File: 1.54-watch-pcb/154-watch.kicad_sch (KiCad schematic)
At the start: 64 parts, among them J1 AFC24-S24FIC-00, J2 Conn_01x06_Female, J3 USB_C_Programming, J4 Jack-DC, J5 Conn_01x02_Male, Q1 Si1308, Q2 BC817, Q3 BC817, Q4 Si2301CDS, SW1 RESET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

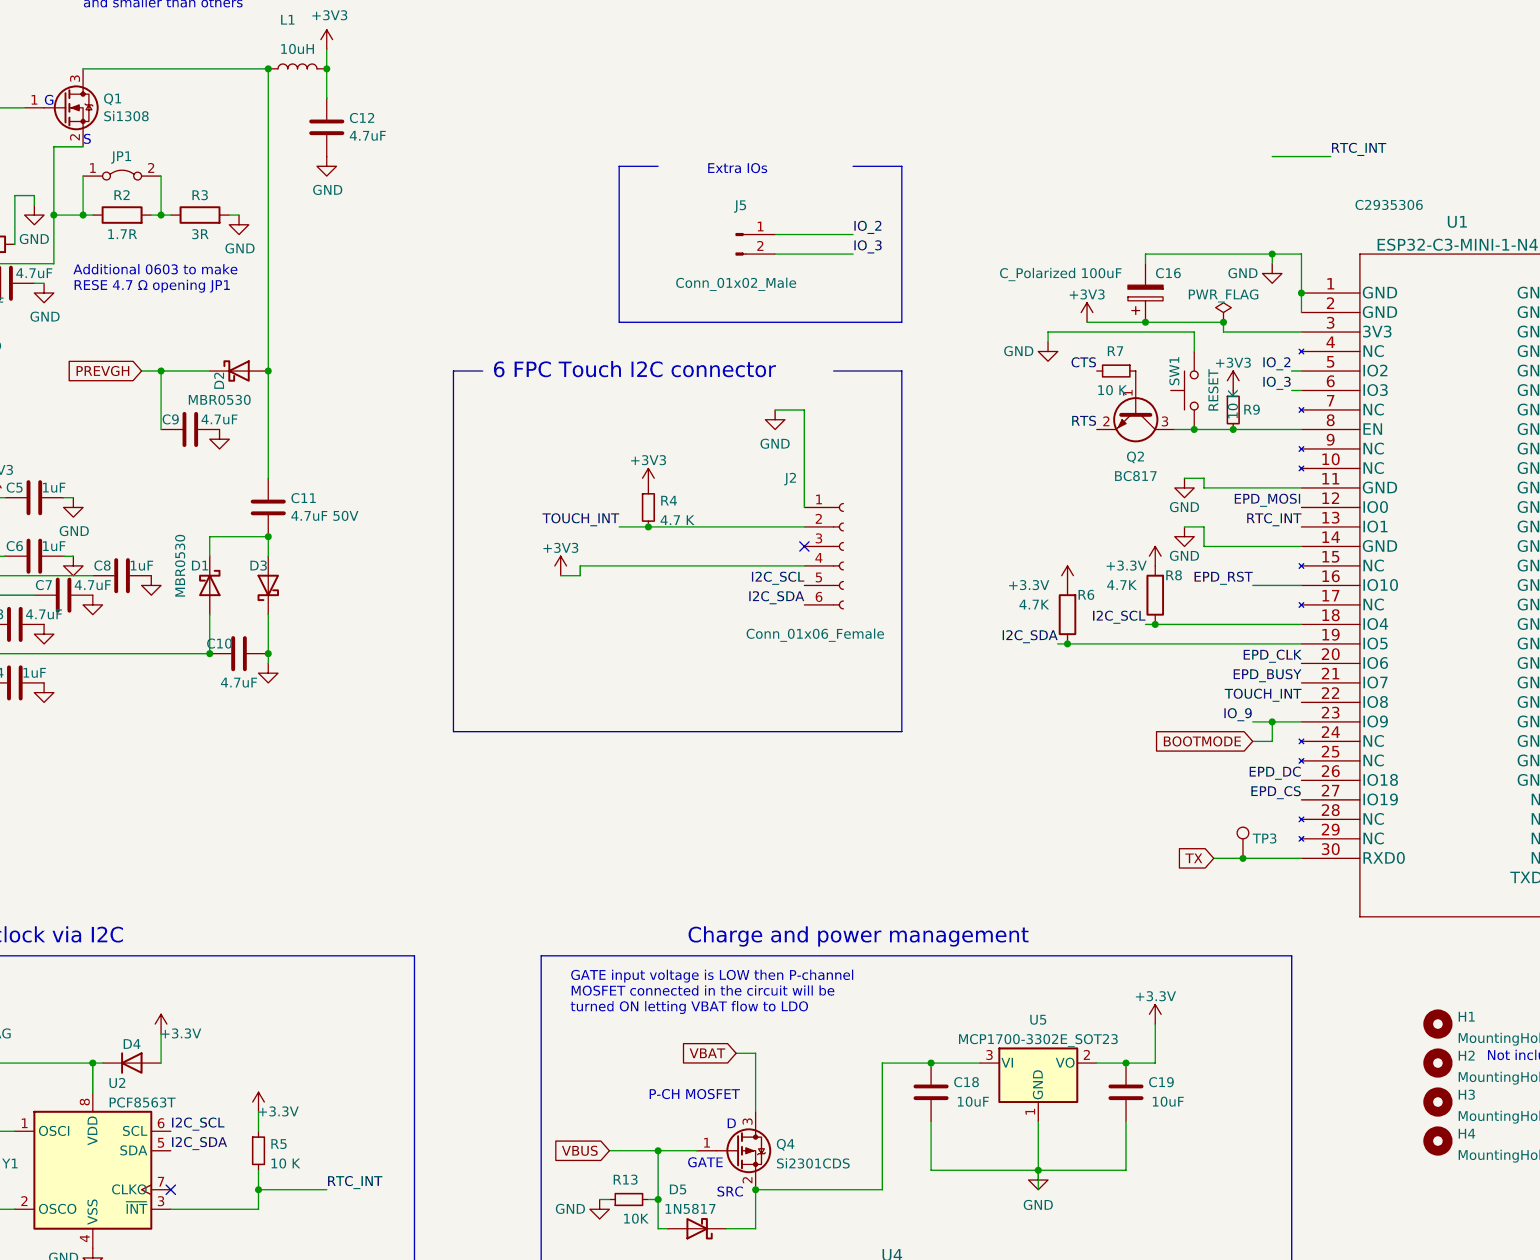
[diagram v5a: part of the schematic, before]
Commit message: First draft of LCD controller, non DRC val #10
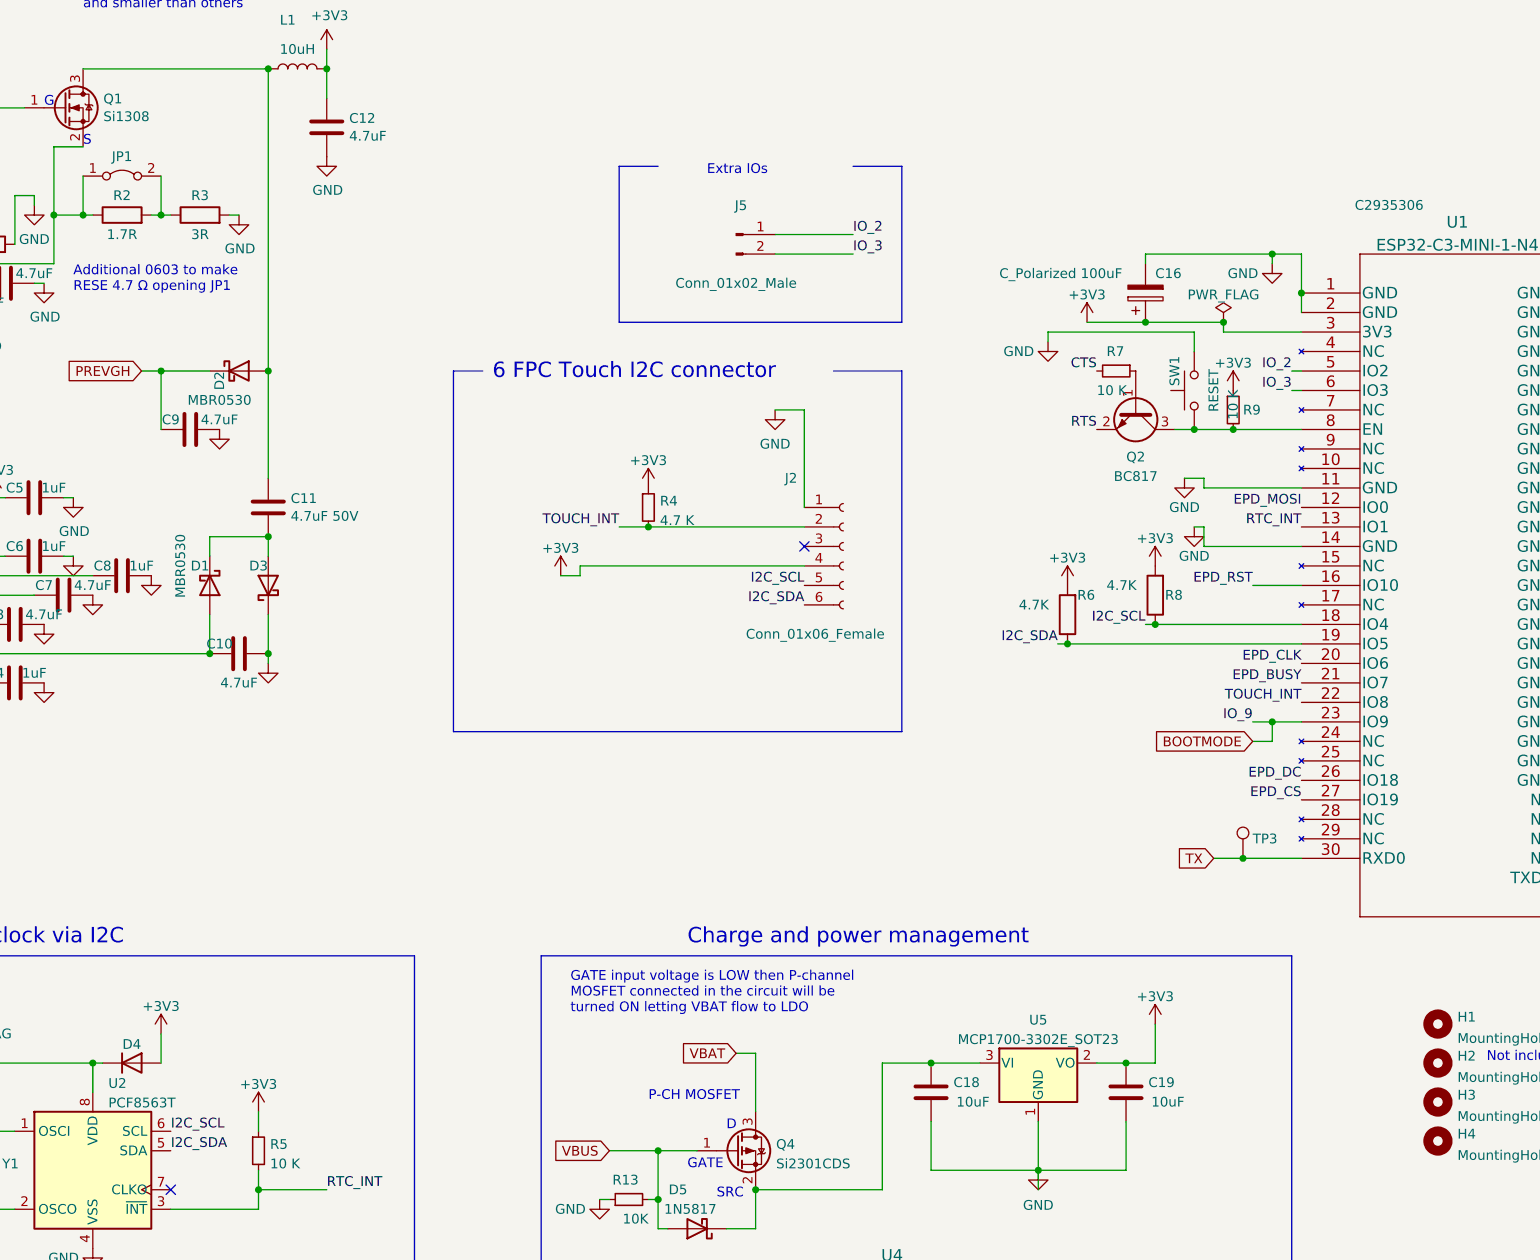
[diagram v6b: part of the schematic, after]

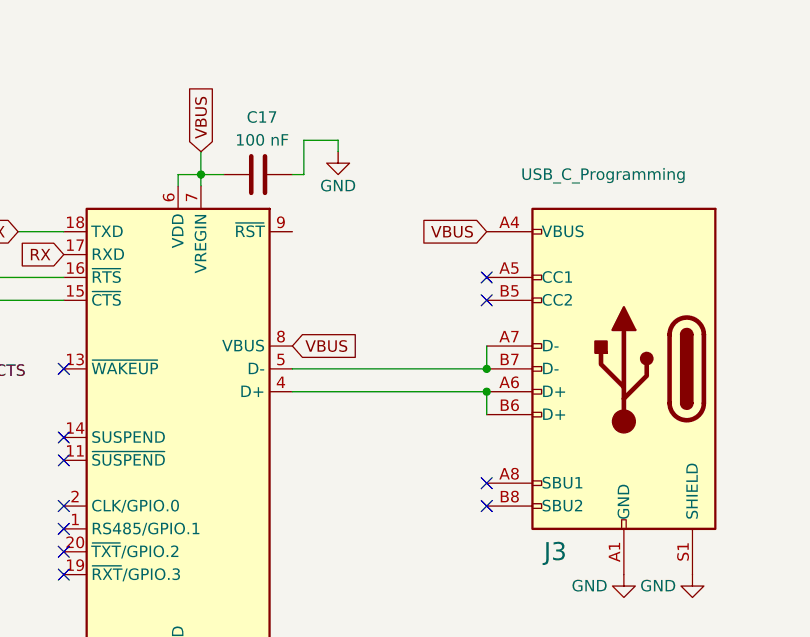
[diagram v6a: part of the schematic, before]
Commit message: Sharp LCD prod. 1.0 and update to failed watch
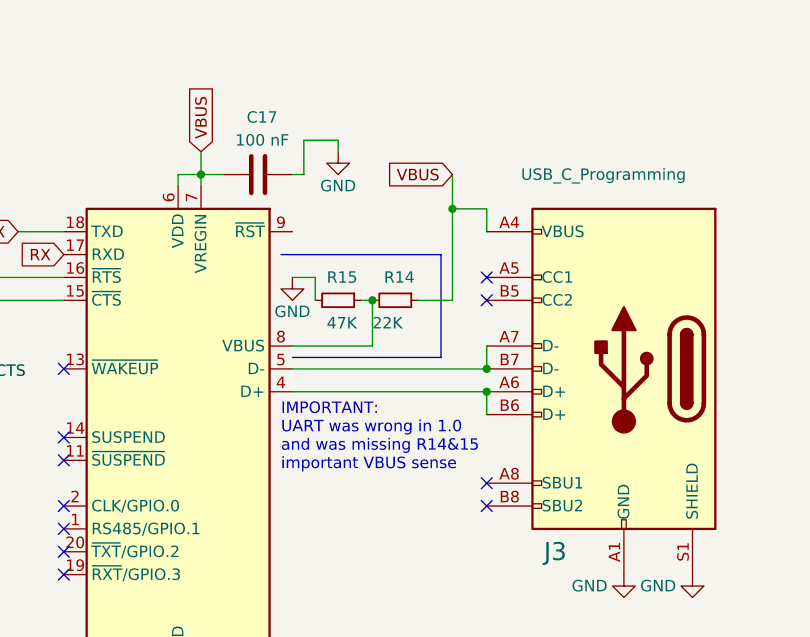
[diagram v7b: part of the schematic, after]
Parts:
- added R14: 22K, Resistor_SMD:R_0603_1608Metric, symbol Device:R_Small
- added R15: 47K, Resistor_SMD:R_0603_1608Metric, symbol Device:R_Small
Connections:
- net GND: now also R15.2
- net VBUS: now also R14.1; no longer U3.8 (VBUS)
- new net: R14.2, R15.1, U3.8 (VBUS)
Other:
- note added: "IMPORTANT: UART was wrong in 1.0 and was missing R14&15 important VBUS sense"
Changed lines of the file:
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@@
   (junction (at 281.94 92.71) (diameter 0) (color 0 0 0 0)
   )
+  (junction (at 372.11 62.23) (diameter 0) (color 0 0 0 0)
+  )
   (junction (at 281.94 123.19) (diameter 0) (color 0 0 0 0)
   )
@@
   (junction (at 281.94 69.85) (diameter 0) (color 0 0 0 0)
   )
+  (junction (at 363.22 72.39) (diameter 0) (color 0 0 0 0)
+  )
   (junction (at 281.94 67.31) (diameter 0) (color 0 0 0 0)
   )
@@
     (stroke (width 0) (type default))
   )
+  (wire (pts (xy 363.22 72.39) (xy 363.22 77.47))
+    (stroke (width 0) (type default))
+  )
   (wire (pts (xy 69.85 186.69) (xy 73.66 186.69))
     (stroke (width 0) (type default))
@@
     (stroke (width 0) (type default))
   )
+  (wire (pts (xy 372.11 72.39) (xy 372.11 62.23))
+    (stroke (width 0) (type default))
+  )
   (wire (pts (xy 170.18 184.15) (xy 186.69 184.15))
     (stroke (width 0) (type default))
@@
     (stroke (width 0) (type default))
   )
+  (wire (pts (xy 375.92 62.23) (xy 375.92 64.77))
+    (stroke (width 0) (type default))
+  )
   (wire (pts (xy 241.3 62.23) (xy 237.49 62.23))
     (stroke (width 0) (type default))
@@
     (stroke (width 0) (type default))
   )
+  (wire (pts (xy 372.11 58.42) (xy 372.11 62.23))
+    (stroke (width 0) (type default))
+  )
   (wire (pts (xy 170.18 189.23) (xy 170.18 184.15))
     (stroke (width 0) (type default))
@@
     (stroke (width 0) (type default))
   )
+  (wire (pts (xy 368.3 72.39) (xy 372.11 72.39))
+    (stroke (width 0) (type default))
+  )
   (wire (pts (xy 222.25 167.64) (xy 222.25 162.56))
     (stroke (width 0) (type default))
@@
     (stroke (width 0) (type default))
   )
+  (polyline (pts (xy 354.33 78.74) (xy 370.84 78.74))
+    (stroke (width 0) (type default))
+  )
   (wire (pts (xy 323.85 64.77) (xy 328.93 64.77))
     (stroke (width 0) (type default))
@@
     (stroke (width 0) (type default))
   )
+  (polyline (pts (xy 370.84 67.31) (xy 370.84 78.74))
+    (stroke (width 0) (type default))
+  )
   (wire (pts (xy 227.33 85.09) (xy 232.41 85.09))
     (stroke (width 0) (type default))
@@
     (stroke (width 0) (type default))
   )
+  (wire (pts (xy 354.33 69.85) (xy 356.87 69.85))
+    (stroke (width 0) (type default))
+  )
   (wire (pts (xy 62.23 93.98) (xy 71.12 93.98))
     (stroke (width 0) (type default))
@@
     (stroke (width 0) (type default))
   )
+  (wire (pts (xy 363.22 77.47) (xy 354.33 77.47))
+    (stroke (width 0) (type default))
+  )
   (wire (pts (xy 281.94 97.79) (xy 281.94 95.25))
     (stroke (width 0) (type default))
@@
     (stroke (width 0) (type default))
   )
+  (wire (pts (xy 372.11 62.23) (xy 375.92 62.23))
+    (stroke (width 0) (type default))
+  )
   (wire (pts (xy 281.94 62.23) (xy 288.29 62.23))
     (stroke (width 0) (type default))
@@
     (stroke (width 0) (type default))
   )
+  (polyline (pts (xy 353.06 67.31) (xy 370.84 67.31))
+    (stroke (width 0) (type default))
+  )
   (polyline (pts (xy 41.91 208.28) (xy 41.91 228.6))
     (stroke (width 0) (type default))
@@
     (stroke (width 0) (type default))
   )
+  (wire (pts (xy 361.95 72.39) (xy 363.22 72.39))
+    (stroke (width 0) (type default))
+  )
   (polyline (pts (xy 240.03 220.98) (xy 240.03 153.67))
     (stroke (width 0) (type default))
@@
     (stroke (width 0) (type default))
   )
+  (wire (pts (xy 356.87 69.85) (xy 356.87 72.39))
+    (stroke (width 0) (type default))
+  )
   (wire (pts (xy 58.42 60.96) (xy 66.04 60.96))
     (stroke (width 0) (type default))
@@
     (effects (font (size 1.27 1.27)) (justify left bottom))
   )
+  (text "IMPORTANT:\nUART was wrong in 1.0\nand was missing R14&15\nimportant VBUS sense"
+    (at 353.06 91.44 0)
+    (effects (font (size 1.27 1.27)) (justify left bottom))
+  )
   (text "Charge and power management" (at 161.29 152.4 0)
     (effects (font (size 2 2)) (justify left bottom))
@@
     )
   )
-  (global_label "VBUS" (shape input) (at 375.92 64.77 180) (fields_autoplaced)
+  (global_label "VBUS" (shape input) (at 372.11 58.42 180) (fields_autoplaced)
     (effects (font (size 1.27 1.27)) (justify right))
-    (property "Intersheetrefs" "${INTERSHEET_REFS}" (at 368.6083 64.6906 0)
+    (property "Intersheetrefs" "${INTERSHEET_REFS}" (at 364.7983 58.3406 0)
       (effects (font (size 1.27 1.27)) (justify right) hide)
     )
@@
     )
   )
-  (global_label "VBUS" (shape input) (at 354.33 77.47 0) (fields_autoplaced)
-    (effects (font (size 1.27 1.27)) (justify left))
-    (property "Intersheetrefs" "${INTERSHEET_REFS}" (at 361.6417 77.5494 0)
-      (effects (font (size 1.27 1.27)) (justify left) hide)
-    )
-  )
   (global_label "RX" (shape input) (at 328.93 67.31 180) (fields_autoplaced)
     (effects (font (size 1.27 1.27)) (justify right))
@@
     )
   )
+  (symbol (lib_id "Device:R_Small") (at 359.41 72.39 270) (unit 1)
+    (in_bom yes) (on_board yes) (dnp no)
+    (property "Reference" "R15" (at 358.14 69.85 90)
+      (effects (font (size 1.27 1.27)) (justify left))
+    )
+    (property "Value" "47K" (at 358.14 74.93 90)
+      (effects (font (size 1.27 1.27)) (justify left))
+    )
+    (property "Footprint" "Resistor_SMD:R_0603_1608Metric" (at 359.41 72.39 0)
+      (effects (font (size 1.27 1.27)) hide)
+    )
+    (property "Datasheet" "https://jlcpcb.com/partdetail/Yageo-RC0603FR0747K5L/C137715" (at 359.41 72.39 0)
+      (effects (font (size 1.27 1.27)) hide)
+    )
+    (property "LCSC" "C137715" (at 359.41 72.39 90)
+      (effects (font (size 1.27 1.27)) hide)
+    )
+    (pin "1")
+    (pin "2")
+    (instances
+      (project "C3-27-epaper-touch"
+        (path "/42575459-fa0a-4761-8328-0238c17cbdda"
+          (reference "R15") (unit 1)
+        )
+      )
+      (project "154-watch"
+        (path "/ea6fde00-59dc-4a79-a647-7e38199fae0e"
+          (reference "R15") (unit 1)
+        )
+      )
+    )
+  )
   (symbol (lib_id "power:GND") (at 77.47 66.04 0) (unit 1)
     (in_bom yes) (on_board yes) (dnp no)
@@
     )
   )
+  (symbol (lib_id "power:GND") (at 354.33 69.85 0) (unit 1)
+    (in_bom yes) (on_board yes) (dnp no)
+    (property "Reference" "#PWR036" (at 354.33 76.2 0)
+      (effects (font (size 1.27 1.27)) hide)
+    )
+    (property "Value" "GND" (at 354.33 73.66 0)
+      (effects (font (size 1.27 1.27)))
+    )
+    (property "Footprint" "" (at 354.33 69.85 0)
+      (effects (font (size 1.27 1.27)) hide)
+    )
+    (property "Datasheet" "" (at 354.33 69.85 0)
+      (effects (font (size 1.27 1.27)) hide)
+    )
+    (pin "1")
+    (instances
+      (project "154-watch"
+        (path "/ea6fde00-59dc-4a79-a647-7e38199fae0e"
+          (reference "#PWR036") (unit 1)
+        )
+      )
+    )
+  )
   (symbol (lib_id "Diode:MBR0530") (at 106.68 105.41 90) (unit 1)
     (in_bom yes) (on_board yes) (dnp no)
@@
         )
       )
+    )
+  )
+  (symbol (lib_id "Device:R_Small") (at 365.76 72.39 270) (unit 1)
+    (in_bom yes) (on_board yes) (dnp no)
+    (property "Reference" "R14" (at 364.49 69.85 90)
+      (effects (font (size 1.27 1.27)) (justify left))
+    )
+    (property "Value" "22K" (at 363.22 74.93 90)
+      (effects (font (size 1.27 1.27)) (justify left))
+    )
+    (property "Footprint" "Resistor_SMD:R_0603_1608Metric" (at 365.76 72.39 0)
+      (effects (font (size 1.27 1.27)) hide)
+    )
+    (property "Datasheet" "https://jlcpcb.com/partdetail/32812-0603WAF2202T5E/C31850" (at 365.76 72.39 0)
+      (effects (font (size 1.27 1.27)) hide)
+    )
+    (property "LCSC" "C31850" (at 365.76 72.39 90)
+      (effects (font (size 1.27 1.27)) hide)
+    )
+    (pin "1")
+    (pin "2")
+    (instances
+      (project "C3-27-epaper-touch"
+        (path "/42575459-fa0a-4761-8328-0238c17cbdda"
+          (reference "R14") (unit 1)
+        )
+      )
+      (project "154-watch"
+        (path "/ea6fde00-59dc-4a79-a647-7e38199fae0e"
+          (reference "R14") (unit 1)
+        )
+      )
